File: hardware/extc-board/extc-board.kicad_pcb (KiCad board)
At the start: 2 copper layers, 38.5 x 85 mm, 19 parts, among them J1 GH BM07B link to INT, J2 VCC DATA GND, J3 PTSM 0,5/2-HH-2,5-SMD 24 VAC, J4 PTSM 0,5/2-HV-2,5-SMD 5V OUT, U1 DS2482-100, U3 TMR 12-4811WI

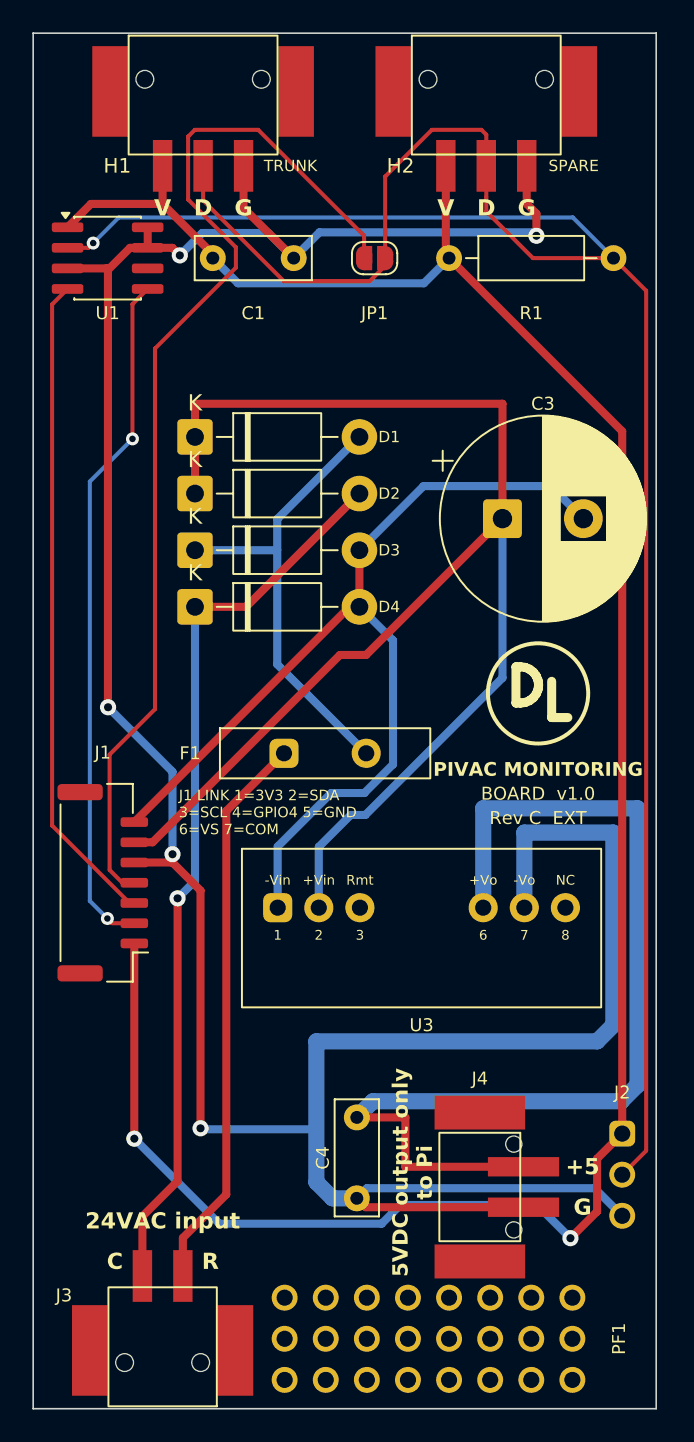
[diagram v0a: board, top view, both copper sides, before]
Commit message: Rev C: fit check against Phoenix's STEP models; anchor pads moved 0.4 mm
hardware/fit-check.py lays the STEP models on the footprints of the
generated board and reports the margin of every solder foot inside its
pad and the play of every peg in its hole. It replaces the check in
KiCad's 3D viewer, and stands in for laying a header on a print until
the headers arrive.

Its first run found the horizontal header's anchor feet 0.1 mm off the
rear of their pads. The pads were placed 0.8 to 6.4 mm from the face; the
feet lie 1.5 to 6.5 mm from it. Phoenix's drawing puts the pad's end
0.2 mm past the start of the signal pads, which I had read as 0.2 mm
short of it. The pads are now 1.2 to 6.8 mm from the face, centred on
the feet with 0.3 mm to spare at each end.

The three STEP models are in hardware/vendor with the housing models.

Co-Authored-By: Claude Fable 5.1 <noreply@anthropic.com>
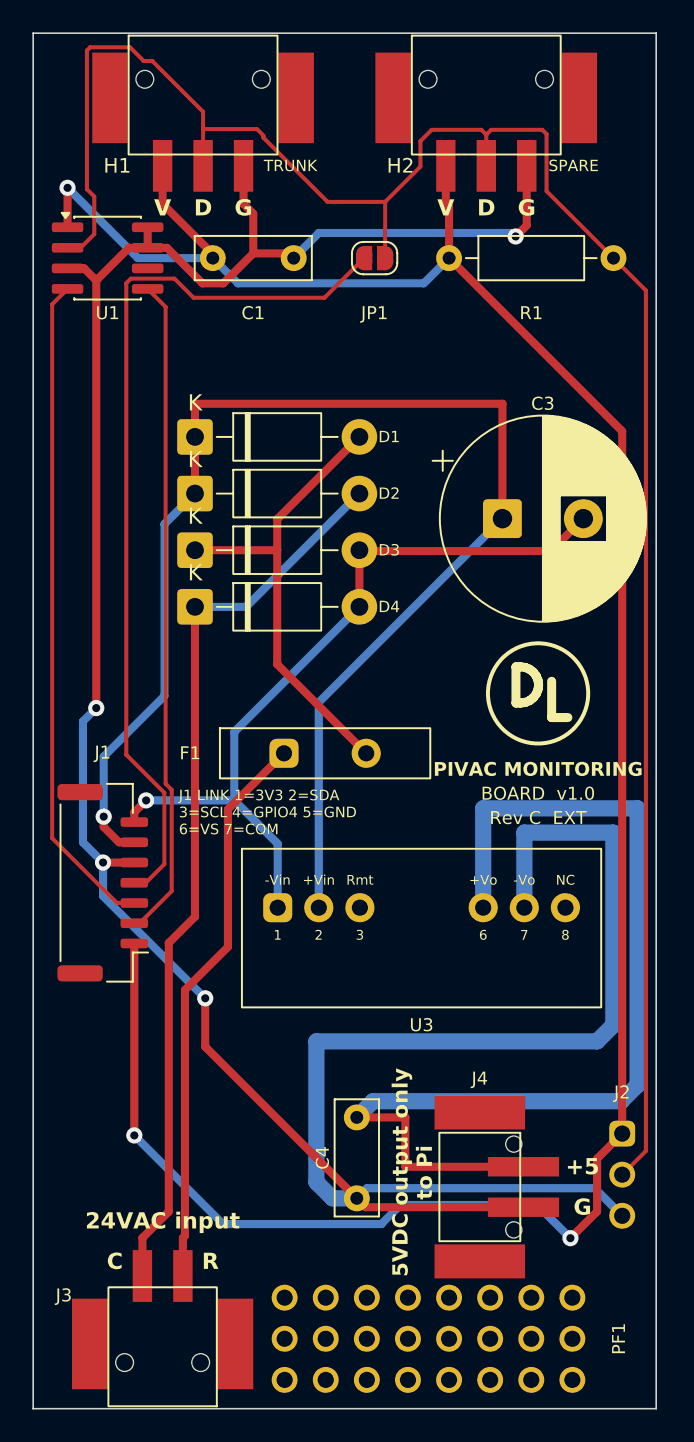
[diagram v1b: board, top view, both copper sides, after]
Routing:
- net COM: track 62.8 -> 48.2 mm, vias 0 -> 1
- net DATA: track 136.4 -> 124.9 mm, vias 1 -> 0
- net GPIO4: track 66.8 -> 55.5 mm
- net VCC: track 144.0 -> 150.6 mm, vias 2 -> 3
- net VS: track 92.0 -> 85.6 mm, vias 0 -> 1
- net SDA: track 42.6 -> 41.0 mm, vias 2 -> 0
- net GND: track 189.8 -> 189.2 mm, vias 5 -> 4
- net ACC: vias 1 -> 0
